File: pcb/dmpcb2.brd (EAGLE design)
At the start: 100 x 100 mm, 74 parts, among them IC1 7805DT, IC2 L293D, IC4 LM358D, IC5 LM358D, J7 SJ-3523-SMT-TR, Q1 IRF530, Q2 IRF530

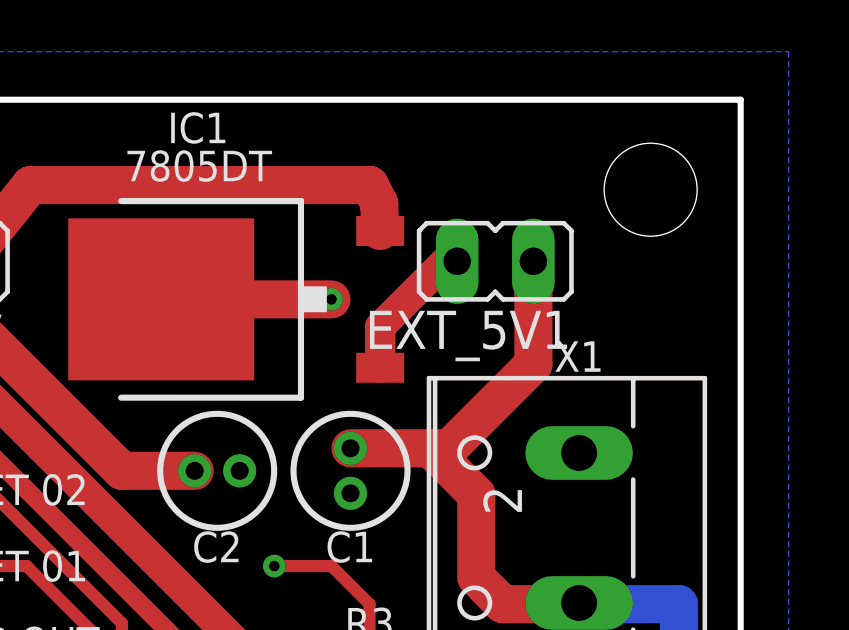
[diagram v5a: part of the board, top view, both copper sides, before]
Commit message: changed naming (v0.2 instead of v.02), some other small fixes
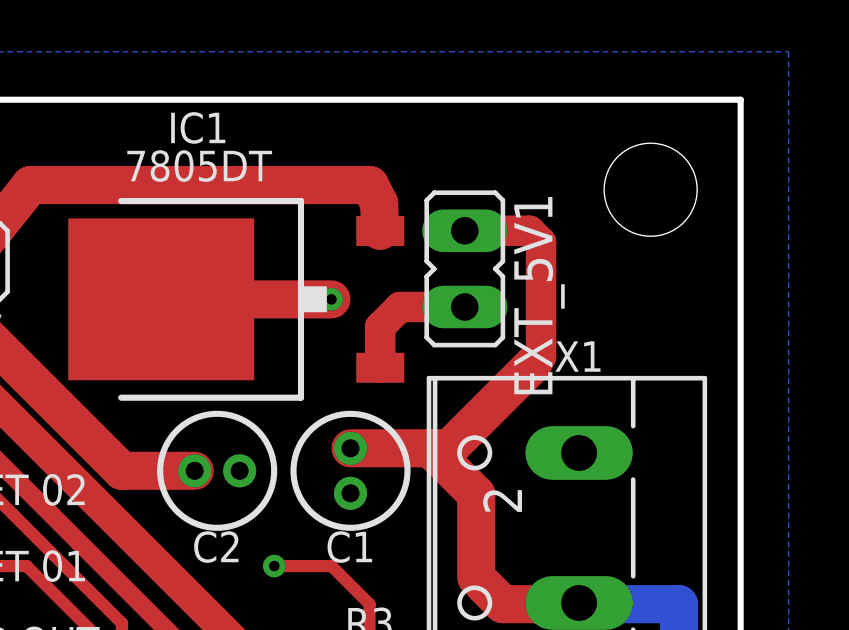
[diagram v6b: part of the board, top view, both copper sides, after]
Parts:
- moved EXT_5V1 1.05 mm to (90.8, 94.4), turned to 180 degrees
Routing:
- net V+: track 223.6 -> 227.0 mm
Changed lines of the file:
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@@
 SENSE.
 MOVE.</text>
+<dimension x1="97.517684375" y1="98.46099375" x2="96.482315625" y2="95.53900625" x3="107.315003125" y3="93.345009375" textsize="1.778" layer="1" dtype="diameter"/>
 </plain>
 <attributes>
@@
 <attribute name="VALUE" x="73.152" y="29.21" size="0.6096" layer="27" font="vector" ratio="20" rot="R270"/>
 </element>
-<element name="EXT_5V1" library="jumper" library_urn="urn:adsk.eagle:library:252" package="JP1" package3d_urn="urn:adsk.eagle:package:15455/1" value="" x="91.821" y="94.615" smashed="yes" rot="R90">
-<attribute name="NAME" x="94.361" y="92.964" size="1.27" layer="25" ratio="10" rot="R180"/>
-<attribute name="POPULARITY" value="61" x="91.821" y="94.615" size="1.778" layer="27" rot="R90" display="off"/>
-<attribute name="VALUE" x="94.361" y="97.536" size="1.27" layer="27" ratio="10" rot="R180"/>
+<element name="EXT_5V1" library="jumper" library_urn="urn:adsk.eagle:library:252" package="JP1" package3d_urn="urn:adsk.eagle:package:15455/1" value="" x="90.805" y="94.361" smashed="yes" rot="R180">
+<attribute name="NAME" x="92.456" y="96.901" size="1.27" layer="25" ratio="10" rot="R270"/>
+<attribute name="POPULARITY" value="61" x="90.805" y="94.361" size="1.778" layer="27" rot="R180" display="off"/>
+<attribute name="VALUE" x="87.884" y="96.901" size="1.27" layer="27" ratio="10" rot="R270"/>
 </element>
 <element name="C5" library="rcl" library_urn="urn:adsk.eagle:library:334" package="C0805" package3d_urn="urn:adsk.eagle:package:23617/2" value="100nf" x="15.24" y="59.69" smashed="yes">
@@
 <wire x1="91.186" y1="84.074" x2="91.44" y2="83.82" width="1.016" layer="1"/>
 <wire x1="91.186" y1="86.844" x2="91.186" y2="84.074" width="1.27" layer="1"/>
-<wire x1="93.091" y1="94.615" x2="93.091" y2="91.186" width="1.27" layer="1"/>
 <wire x1="90.285" y1="88.38" x2="89.65" y2="88.38" width="1.27" layer="1"/>
 <wire x1="93.091" y1="91.186" x2="90.285" y2="88.38" width="1.27" layer="1"/>
@@
 <wire x1="24.765" y1="17.145" x2="22.86" y2="17.145" width="1.27" layer="16"/>
 <wire x1="26.67" y1="3.0226" x2="26.67" y2="15.24" width="1.27" layer="16"/>
+<wire x1="90.805" y1="95.631" x2="92.964" y2="95.631" width="1.016" layer="1"/>
+<wire x1="92.964" y1="95.631" x2="93.345" y2="95.25" width="1.016" layer="1"/>
+<wire x1="93.345" y1="95.25" x2="93.345" y2="91.44" width="1.016" layer="1"/>
+<wire x1="93.345" y1="91.44" x2="93.091" y2="91.186" width="1.016" layer="1"/>
 </signal>
 <signal name="+5V">
@@
 <contactref element="IC1" pad="1"/>
 <wire x1="87.985" y1="91.065" x2="87.985" y2="92.43" width="1.016" layer="1"/>
-<wire x1="90.17" y1="94.615" x2="90.551" y2="94.615" width="1.016" layer="1"/>
-<wire x1="87.985" y1="92.43" x2="90.17" y2="94.615" width="1.016" layer="1"/>
+<wire x1="87.985" y1="92.43" x2="88.646" y2="93.091" width="1.016" layer="1"/>
+<wire x1="88.646" y1="93.091" x2="90.805" y2="93.091" width="1.016" layer="1"/>
 </signal>
 <signal name="OLEDRES">

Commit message: screws fit
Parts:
- added SOCKET_IN1: (no value), con-lstb:MA05-1
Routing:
- net +5V: track 382.7 -> 386.5 mm
- net VMOT: track 22.4 -> 23.3 mm
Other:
- board text added: "JLCJLCJLCJLC"
- board text added: "digital media hfk bremen v0.2"
- board text removed: "digital media bremen hfk bremen v.02"
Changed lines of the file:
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@@
 <text x="57.785" y="55.88" size="1.016" layer="25" align="center-left">AUDIO_OUT</text>
 <text x="57.785" y="58.42" size="1.016" layer="25" align="center-left">A14/DAC</text>
-<text x="79.375" y="5.08" size="1.016" layer="25" font="vector">digital media bremen
-hfk bremen v.02</text>
+<text x="79.375" y="5.08" size="1.016" layer="25" font="vector">digital media
+hfk bremen v0.2</text>
 <polygon width="0.4064" layer="25">
 <vertex x="100.33" y="11.43"/>
@@
 SENSE.
 MOVE.</text>
-<dimension x1="97.517684375" y1="98.46099375" x2="96.482315625" y2="95.53900625" x3="107.315003125" y3="93.345009375" textsize="1.778" layer="1" dtype="diameter"/>
+<text x="46.99" y="69.85" size="1.016" layer="25" rot="R90">JLCJLCJLCJLC</text>
 </plain>
 <attributes>
@@
 </element>
 <element name="DRV8825" library="alvarop-lib" library_urn="urn:adsk.eagle:library:9906355" package="POLOLU-DRV8825" package3d_urn="urn:adsk.eagle:package:9906364/1" value="POLOLU-DRV8825" x="19.05" y="29.21" smashed="yes" rot="R180"/>
-<element name="TEENSY3.2" library="Teensy_3_and_LC_Series_Boards_v1.4" package="TEENSY_3.0-3.2_ALL_PINS_&amp;_PADS" value="TEENSY_3.1-3.2_ALL_PINS&amp;PADS" x="50.53" y="78.105" smashed="yes">
-<attribute name="VALUE" x="46.72" y="83.185" size="1.27" layer="27" font="vector"/>
-</element>
+<element name="TEENSY3.2" library="Teensy_3_and_LC_Series_Boards_v1.4" package="TEENSY_3.0-3.2_ALL_PINS_&amp;_PADS" value="TEENSY_3.1-3.2_ALL_PINS&amp;PADS" x="50.53" y="78.105" smashed="yes"/>
 <element name="JP4" library="jumper" library_urn="urn:adsk.eagle:library:252" package="JP2" package3d_urn="urn:adsk.eagle:package:15452/1" value="" x="21.59" y="45.085" smashed="yes" rot="R90">
 <attribute name="POPULARITY" value="34" x="21.59" y="45.085" size="1.778" layer="27" rot="R90" display="off"/>
@@
 </element>
 <element name="SV2" library="SparkFun-Connectors" library_urn="urn:adsk.eagle:library:513" package="1X12" package3d_urn="urn:adsk.eagle:package:38169/1" value="" x="32.385" y="89.535" smashed="yes" rot="R270">
-<attribute name="NAME" x="34.163" y="104.775" size="1.27" layer="25" ratio="10" rot="R270"/>
 <attribute name="VALUE" x="29.464" y="88.138" size="1.27" layer="27" ratio="10" rot="R270"/>
 </element>
@@
 <attribute name="POPULARITY" value="88" x="43.815" y="33.02" size="1.778" layer="27" rot="R180" display="off"/>
 <attribute name="SPICEPREFIX" value="C" x="43.815" y="33.02" size="1.778" layer="27" rot="R180" display="off"/>
+</element>
+<element name="SOCKET_IN1" library="con-lstb" library_urn="urn:adsk.eagle:library:162" package="MA05-1" package3d_urn="urn:adsk.eagle:package:8332/1" value="" x="50" y="15.494" smashed="yes">
+<attribute name="MF" value="" x="50" y="15.494" size="1.778" layer="27" display="off"/>
+<attribute name="MPN" value="" x="50" y="15.494" size="1.778" layer="27" display="off"/>
+<attribute name="OC_FARNELL" value="unknown" x="50" y="15.494" size="1.778" layer="27" display="off"/>
+<attribute name="OC_NEWARK" value="unknown" x="50" y="15.494" size="1.778" layer="27" display="off"/>
+<attribute name="POPULARITY" value="29" x="50" y="15.494" size="1.778" layer="27" display="off"/>
+<attribute name="VALUE" x="47.46" y="12.573" size="1.27" layer="27" ratio="10"/>
 </element>
 </elements>
@@
 <wire x1="86.995" y1="66.675" x2="86.995" y2="64.135" width="1.016" layer="1"/>
 <wire x1="86.995" y1="66.675" x2="89.535" y2="66.675" width="1.016" layer="1"/>
+<wire x1="44.92" y1="45.72" x2="44.92" y2="47.625" width="0.4064" layer="16"/>
+<wire x1="44.92" y1="45.72" x2="44.92" y2="47.625" width="0.4064" layer="16"/>
 </signal>
 <signal name="MM92">
@@
 <wire x1="6.985" y1="15.875" x2="13.97" y2="15.875" width="1.27" layer="16"/>
 <contactref element="JP1" pad="2"/>
-<wire x1="13.97" y1="15.875" x2="15.92443125" y2="15.875" width="0.6096" layer="1"/>
-<wire x1="15.92443125" y1="15.875" x2="16.55943125" y2="15.24" width="0.6096" layer="1"/>
-<wire x1="16.55943125" y1="15.24" x2="19.685" y2="15.24" width="0.6096" layer="1"/>
-<wire x1="19.685" y1="15.24" x2="20.32" y2="15.875" width="0.6096" layer="1"/>
-<wire x1="20.32" y1="15.875" x2="20.32" y2="17.145" width="0.6096" layer="1"/>
+<wire x1="13.97" y1="15.875" x2="15.875" y2="15.875" width="1.016" layer="1"/>
+<wire x1="15.875" y1="15.875" x2="17.145" y2="14.605" width="1.016" layer="1"/>
+<wire x1="17.145" y1="14.605" x2="19.685" y2="14.605" width="1.016" layer="1"/>
+<wire x1="19.685" y1="14.605" x2="20.32" y2="15.24" width="1.016" layer="1"/>
+<wire x1="20.32" y1="15.24" x2="20.32" y2="17.145" width="1.016" layer="1"/>
 </signal>
 <signal name="DNC">

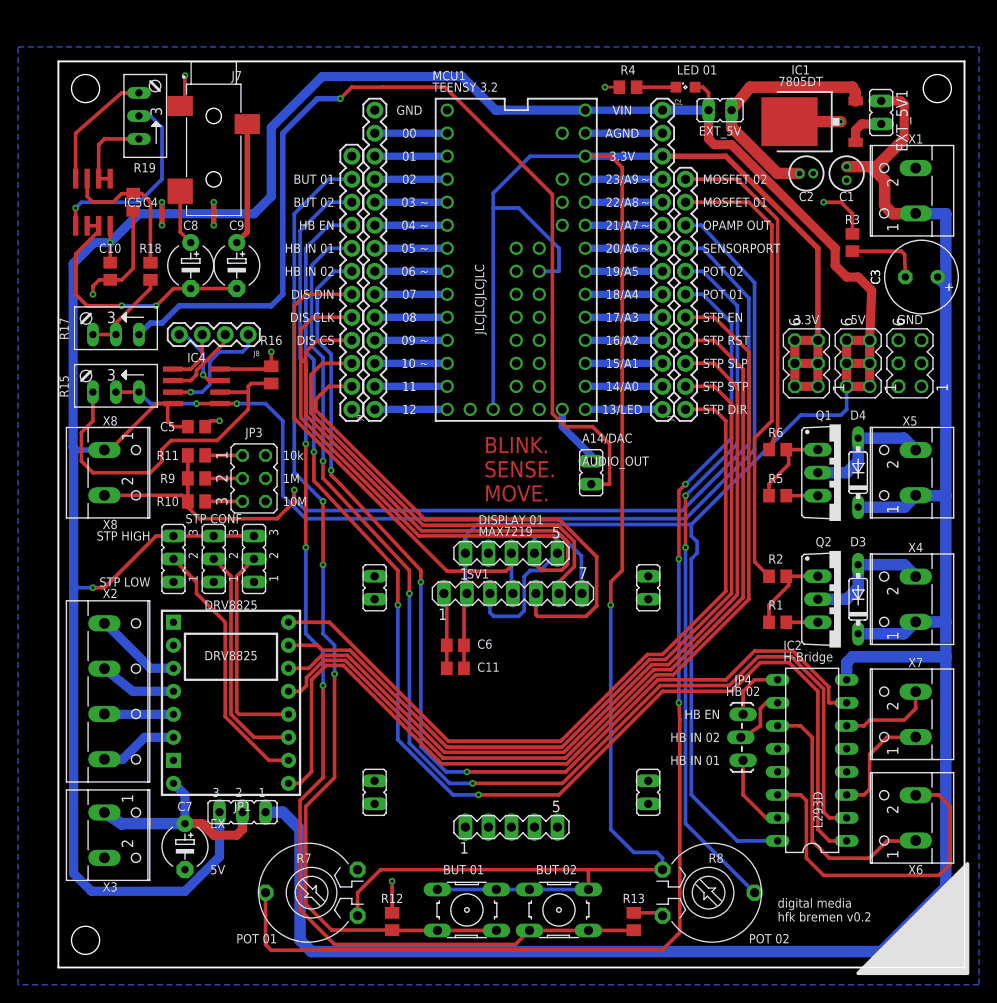
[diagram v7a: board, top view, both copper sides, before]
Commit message: added user leds and labeling for opamp
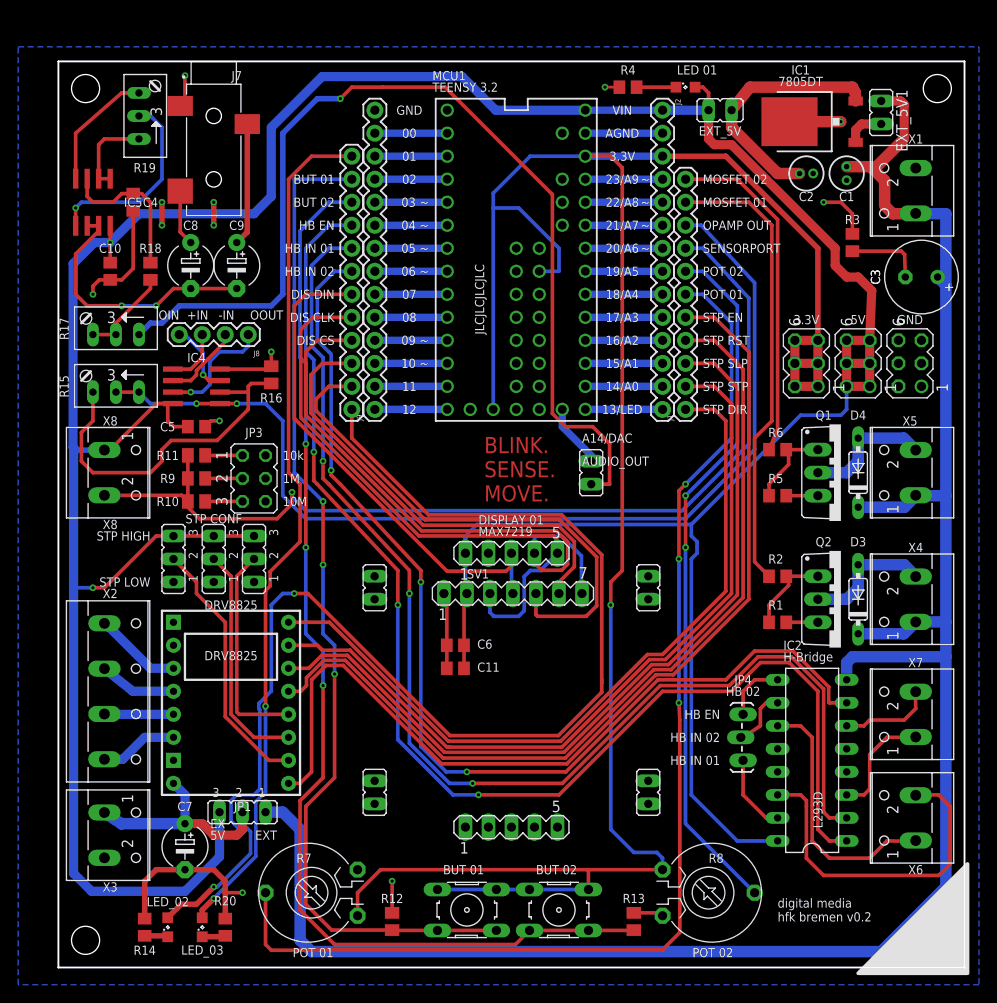
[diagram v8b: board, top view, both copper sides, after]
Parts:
- added LED_02, LED_03: (no value), led:SML0805
- added R14, R20: 220R, rcl:R0805
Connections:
- new net LED1: LED_02.A, SV2.12
- new net LED2: LED_03.A, SV2.1
- new net N$64: LED_02.C, R14.2
- new net N$76: LED_03.C, R20.2
- net GND: now also R14.1, R20.1
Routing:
- net LED1: track 0.00 -> 140.7 mm, vias 0 -> 2
- net LED2: track 0.00 -> 94.5 mm, vias 0 -> 2
- net GND: track 79.4 -> 99.5 mm, vias 12 -> 13
- net N$76: track 0.00 -> 2.58 mm
- net N$64: track 0.00 -> 2.58 mm
- net BUTTON01: track 109.5 -> 111.7 mm
- net SENSORPORT: track 109.8 -> 109.3 mm
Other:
- board text added: "+IN"
- board text added: "-IN"
- board text added: "EXT"
- board text added: "OIN"
- board text added: "OOUT"
